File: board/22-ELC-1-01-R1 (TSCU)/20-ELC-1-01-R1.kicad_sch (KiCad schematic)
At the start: 10 parts, among them J1 Conn_01x116, J2 Conn_01x01, J3 Conn_01x06, J4 Conn_01x02, J5 Conn_01x02, J6 Conn_01x06, J7 Conn_01x01, U9 STM32F105RCTx

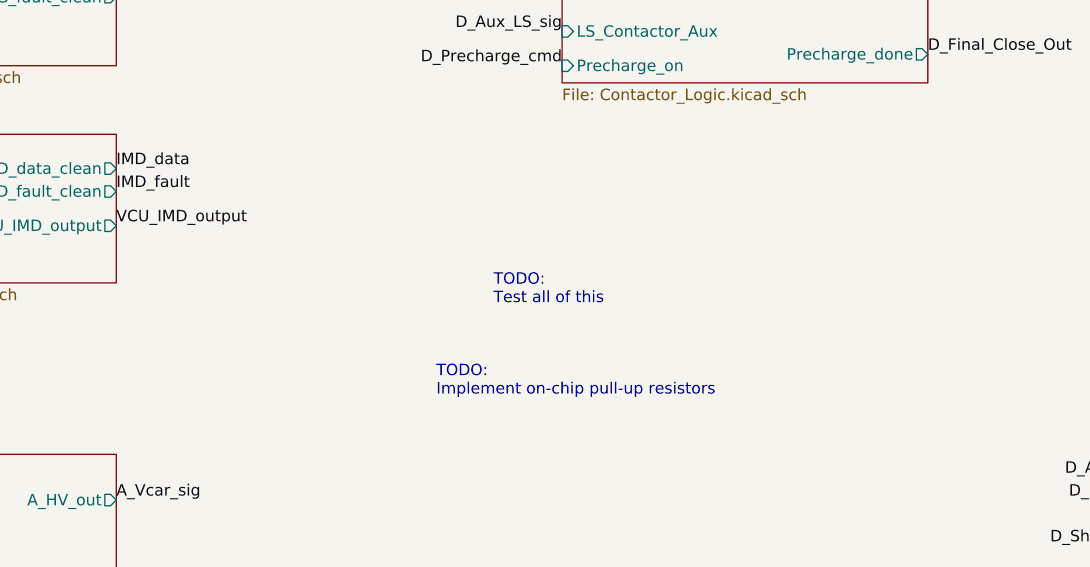
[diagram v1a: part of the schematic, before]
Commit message: Added few LEDs
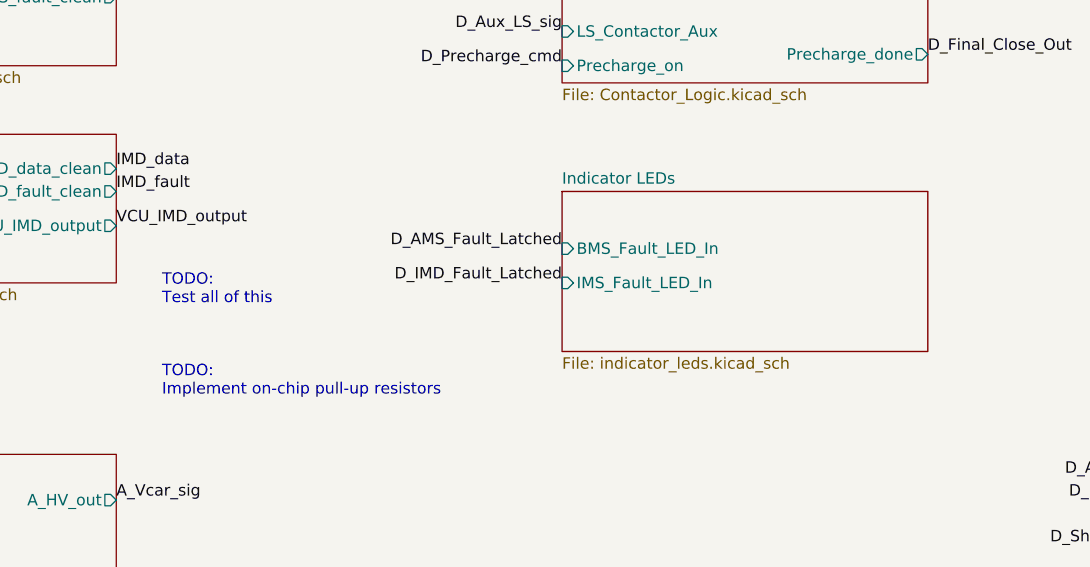
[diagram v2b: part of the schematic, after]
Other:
- added sheet Indicator LEDs (indicator_leds.kicad_sch)
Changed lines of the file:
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@@
     (stroke (width 0) (type default) (color 0 0 0 0))
   )
-  (text "TODO:\nTest all of this" (at 146.05 110.49 0)
+  (text "TODO:\nTest all of this" (at 109.22 110.49 0)
     (effects (font (size 1.27 1.27)) (justify left bottom))
   )
@@
     (effects (font (size 1.27 1.27)) (justify left bottom))
   )
-  (text "TODO:\nImplement on-chip pull-up resistors\n" (at 139.7 120.65 0)
+  (text "TODO:\nImplement on-chip pull-up resistors\n" (at 109.22 120.65 0)
     (effects (font (size 1.27 1.27)) (justify left bottom))
   )
@@
     (effects (font (size 1.27 1.27)) (justify right bottom))
   )
+  (label "D_AMS_Fault_Latched" (at 153.67 104.14 180)
+    (effects (font (size 1.27 1.27)) (justify right bottom))
+  )
   (label "dcdc_enable" (at 104.14 55.88 0)
     (effects (font (size 1.27 1.27)) (justify left bottom))
@@
   (label "IMD_KE" (at 29.21 116.84 0)
     (effects (font (size 1.27 1.27)) (justify left bottom))
+  )
+  (label "D_IMD_Fault_Latched" (at 153.67 107.95 180)
+    (effects (font (size 1.27 1.27)) (justify right bottom))
   )
   (label "D_Final_Close_Out" (at 194.31 82.55 0)
@@
     )
   )
+  (sheet (at 153.67 97.79) (size 40.64 17.78) (fields_autoplaced)
+    (stroke (width 0.1524) (type solid) (color 0 0 0 0))
+    (fill (color 0 0 0 0.0000))
+    (property "Sheet name" "Indicator LEDs" (id 0) (at 153.67 97.0784 0)
+      (effects (font (size 1.27 1.27)) (justify left bottom))
+    )
+    (property "Sheet file" "indicator_leds.kicad_sch" (id 1) (at 153.67 116.1546 0)
+      (effects (font (size 1.27 1.27)) (justify left top))
+    )
+    (pin "BMS_Fault_LED_In" input (at 153.67 104.14 180)
+      (effects (font (size 1.27 1.27)) (justify left))
+    )
+    (pin "IMS_Fault_LED_In" input (at 153.67 107.95 180)
+      (effects (font (size 1.27 1.27)) (justify left))
+    )
+  )
   (sheet_instances
     (path "/" (page "1"))
@@
     (path "/00000000-0000-0000-0000-00005d90d733" (page "11"))
     (path "/00000000-0000-0000-0000-000060f65a9c" (page "12"))
+    (path "/28d99f6e-a836-4db6-bc71-c35494bde910" (page "13"))
   )
   (symbol_instances
@@
       (reference "#PWR0106") (unit 1) (value "+5V") (footprint "")
     )
+    (path "/28d99f6e-a836-4db6-bc71-c35494bde910/24de73d2-9209-4edd-bd8a-39acaaf3a98b"
+      (reference "#PWR?") (unit 1) (value "GND") (footprint "")
+    )
+    (path "/28d99f6e-a836-4db6-bc71-c35494bde910/272d79de-c897-47ec-8cee-bdc709f98f7e"
+      (reference "#PWR?") (unit 1) (value "GND") (footprint "")
+    )
+    (path "/28d99f6e-a836-4db6-bc71-c35494bde910/90973fb4-d197-4463-9118-c7a94f62c78f"
+      (reference "#PWR?") (unit 1) (value "GND") (footprint "")
+    )
+    (path "/00000000-0000-0000-0000-0000617aed82/e9347cbc-281d-4d89-87e3-40eb1e5413f4"
+      (reference "#PWR?") (unit 1) (value "+5V") (footprint "")
+    )
+    (path "/28d99f6e-a836-4db6-bc71-c35494bde910/f395fc8e-933f-4544-83d1-7f8405023da7"
+      (reference "#PWR?") (unit 1) (value "+5V") (footprint "")
+    )
     (path "/00000000-0000-0000-0000-000060ed073e"
       (reference "A1") (unit 1) (value "Arduino_Nano_v3.x") (footprint "Module:Arduino_Nano")
@@
       (reference "D10") (unit 1) (value "B5819W") (footprint "Diode_SMD:D_SOD-123")
     )
+    (path "/00000000-0000-0000-0000-0000617aed82/3efac1eb-81f2-40fb-ac97-158176863b6e"
+      (reference "D?") (unit 1) (value "BMS_STATUS") (footprint "")
+    )
+    (path "/28d99f6e-a836-4db6-bc71-c35494bde910/5e5dc036-0bed-43f1-a5de-67433ad83c36"
+      (reference "D?") (unit 1) (value "BMS_FAULT_LED") (footprint "")
+    )
+    (path "/28d99f6e-a836-4db6-bc71-c35494bde910/dc6f94e1-4680-4b48-ace0-d6d0f492507b"
+      (reference "D?") (unit 1) (value "IMS_FAULT_LED") (footprint "")
+    )
     (path "/00000000-0000-0000-0000-00005d90d7d4/00000000-0000-0000-0000-00006038728c"
       (reference "F2") (unit 1) (value "2A") (footprint "Fuse:Fuse_1206_3216Metric_Pad1.42x1.75mm_HandSolder")
@@
       (reference "R51") (unit 1) (value "1k") (footprint "Resistor_SMD:R_0603_1608Metric_Pad0.98x0.95mm_HandSolder")
     )
+    (path "/28d99f6e-a836-4db6-bc71-c35494bde910/adac11e5-2860-40e4-bce4-e19a3e8a583d"
+      (reference "R?") (unit 1) (value "220") (footprint "")
+    )
+    (path "/00000000-0000-0000-0000-0000617aed82/b2b589bf-c37f-42c7-8186-328578765787"
+      (reference "R?") (unit 1) (value "220") (footprint "")
+    )
+    (path "/28d99f6e-a836-4db6-bc71-c35494bde910/eedced55-176a-45b3-a3da-bff1a25d967f"
+      (reference "R?") (unit 1) (value "220") (footprint "")
+    )
     (path "/00000000-0000-0000-0000-000060f320ba/00000000-0000-0000-0000-0000600d193f"
       (reference "RV1") (unit 1) (value "R_POT_TRIM") (footprint "Potentiometer_THT:Potentiometer_Bourns_3296W_Vertical")
@@
       (reference "TP18") (unit 1) (value "TestPoint") (footprint "TestPoint:TestPoint_THTPad_D1.0mm_Drill0.5mm")
     )
+    (path "/00000000-0000-0000-0000-00005d90d733/ebf6a852-e42b-44f6-a1de-740340178ead"
+      (reference "TP?") (unit 1) (value "TestPoint") (footprint "")
+    )
     (path "/00000000-0000-0000-0000-00005d9ae4f9/00000000-0000-0000-0000-000060f3ae0d"
       (reference "U1") (unit 1) (value "TPS5430DDA") (footprint "Package_SO:TI_SO-PowerPAD-8_ThermalVias")
@@
       (reference "U14") (unit 3) (value "LM358") (footprint "Package_SO:SOIC-8_3.9x4.9mm_P1.27mm")
     )
+    (path "/28d99f6e-a836-4db6-bc71-c35494bde910/99db8223-dc3d-4d3f-8640-b6a4b37188a4"
+      (reference "U?") (unit 1) (value "LM358") (footprint "")
+    )
+    (path "/28d99f6e-a836-4db6-bc71-c35494bde910/e0bcac9d-dab7-4abe-89f1-620c9ec5fd7a"
+      (reference "U?") (unit 1) (value "LM358") (footprint "")
+    )
+    (path "/28d99f6e-a836-4db6-bc71-c35494bde910/13ca8184-2714-4986-b99a-1f20e984bbea"
+      (reference "U?") (unit 2) (value "LM358") (footprint "")
+    )
+    (path "/28d99f6e-a836-4db6-bc71-c35494bde910/6a060a57-d1e4-464a-b390-6294ef420732"
+      (reference "U?") (unit 3) (value "LM358") (footprint "")
+    )
     (path "/00000000-0000-0000-0000-000060f545d6/00000000-0000-0000-0000-000060f58487"

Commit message: More work
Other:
- added sheet Untitled Sheet (../../2023KicadLibrary/Standardized Subsheets/microcontroller.kicad_sch)

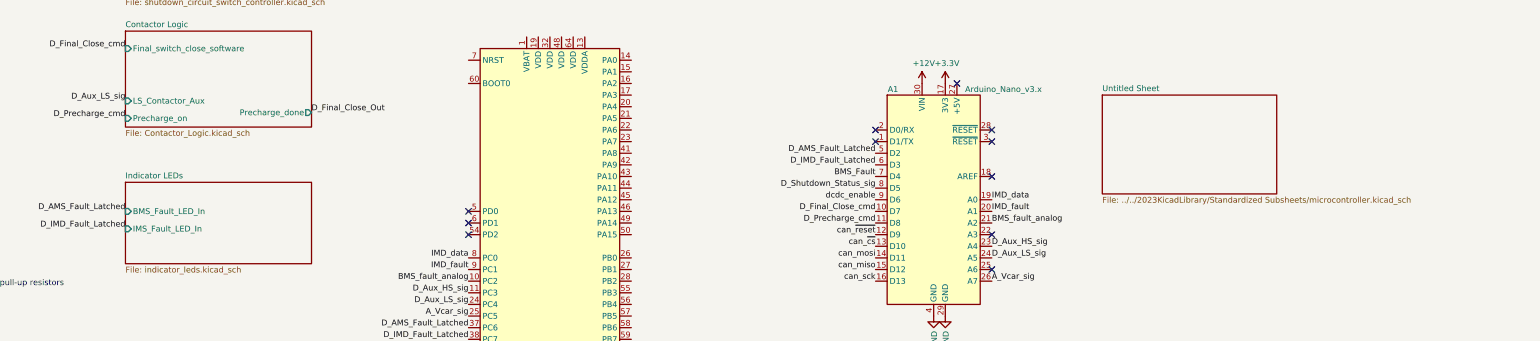
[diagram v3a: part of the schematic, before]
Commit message: More LEDs and test points
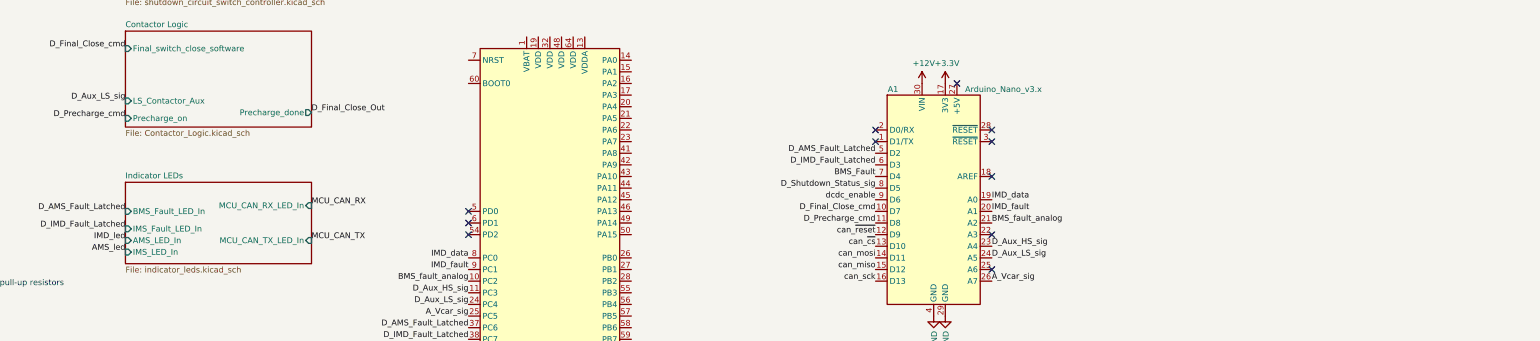
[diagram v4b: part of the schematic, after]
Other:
- removed sheet Untitled Sheet
- sheet Indicator LEDs ports: added AMS_LED_In, IMS_LED_In, MCU_CAN_RX_LED_In, MCU_CAN_TX_LED_In; removed none

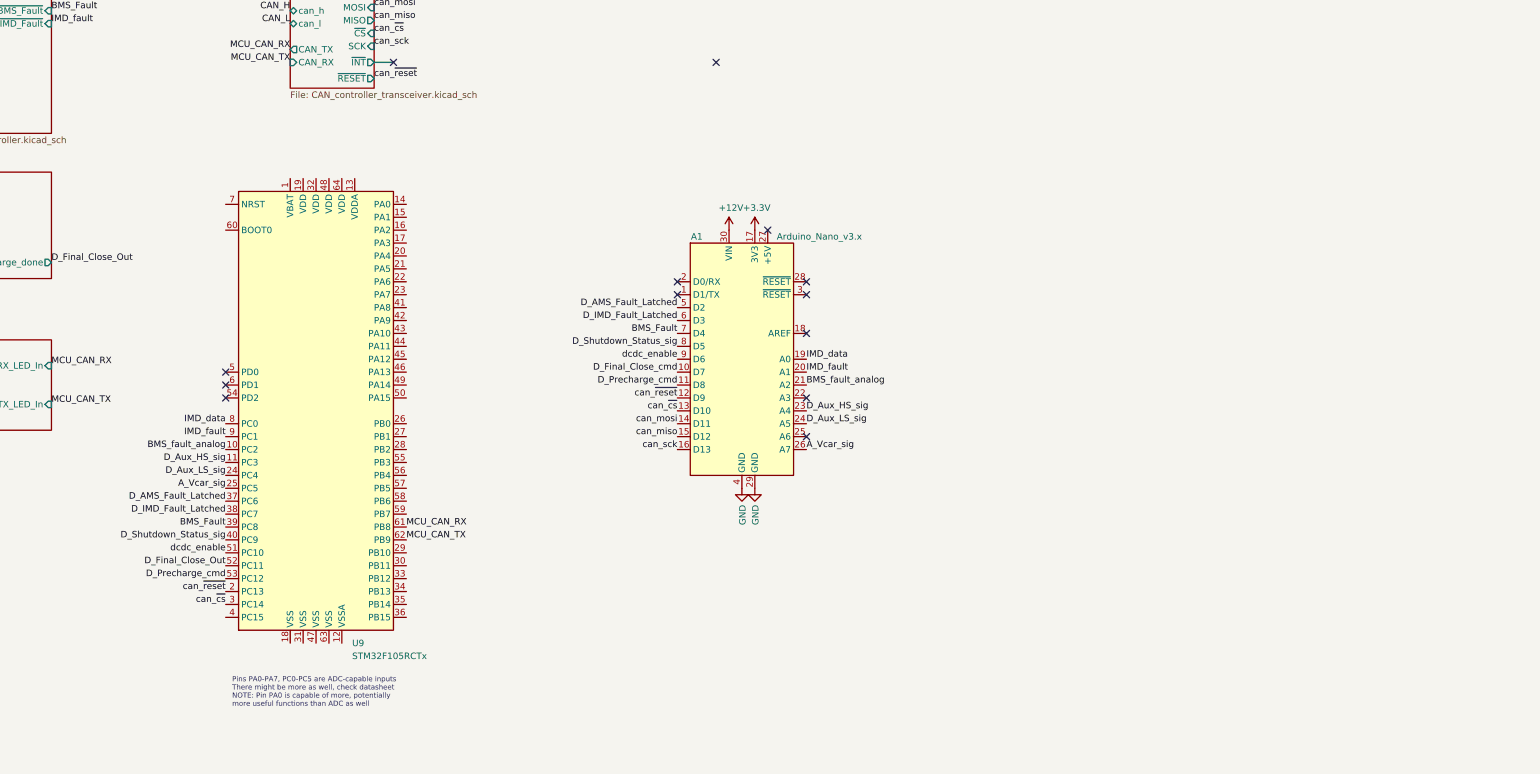
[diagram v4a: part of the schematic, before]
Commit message: More LEDs and TPs
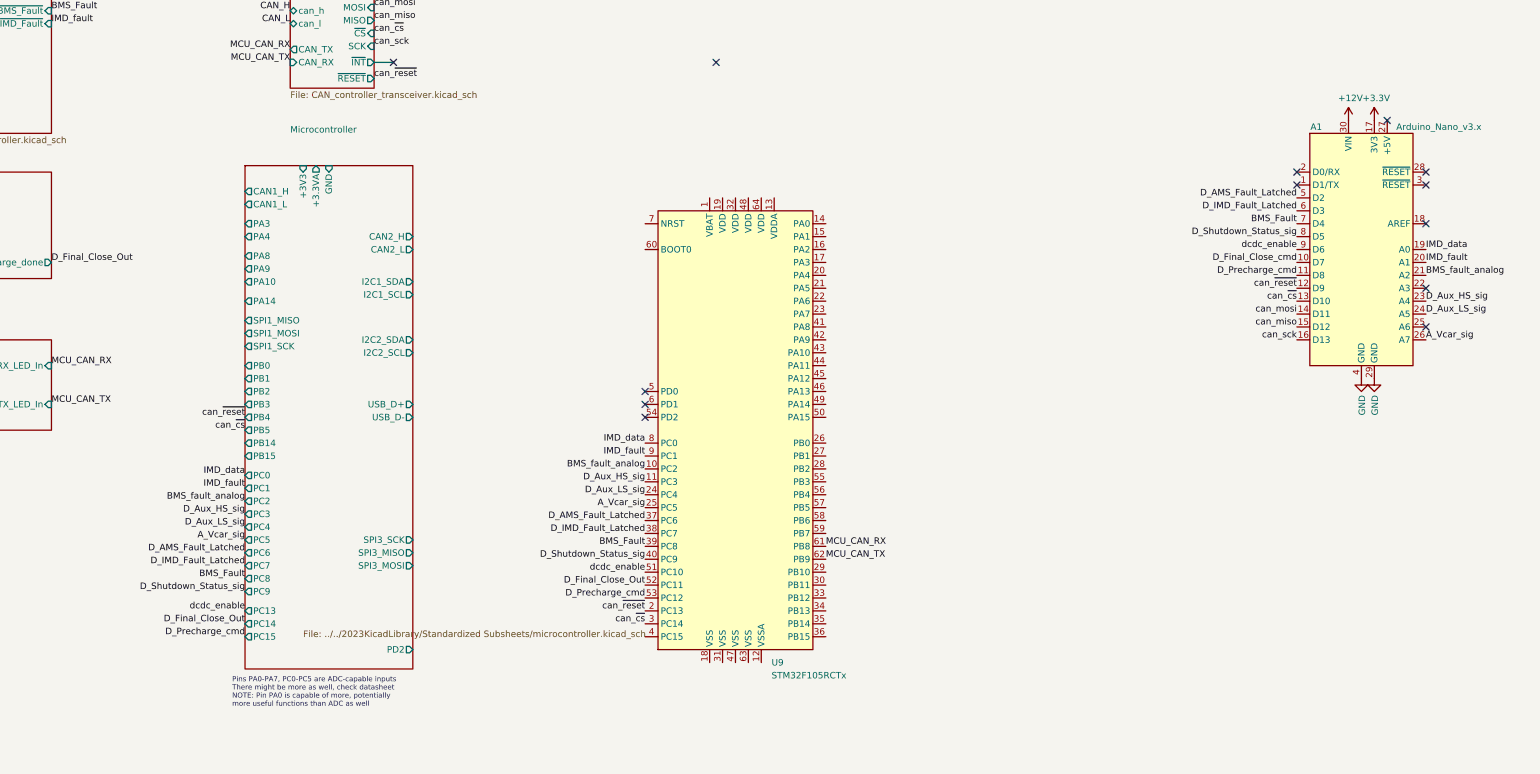
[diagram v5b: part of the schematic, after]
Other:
- added sheet Microcontroller (../../2023KicadLibrary/Standardized Subsheets/microcontroller.kicad_sch)
- moved on the sheet: A1, U9

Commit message: Ready for review
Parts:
- removed A1: Arduino_Nano_v3.x, Module:Arduino_Nano, symbol MCU_Module:Arduino_Nano_v2.x
- removed U9: STM32F105RCTx, Package_QFP:LQFP-64_10x10mm_P0.5mm, symbol MCU_ST_STM32F1:STM32F105RCTx
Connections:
- no-connect marks 15 -> 33
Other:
- added sheet 3V3Supply (../../2023KicadLibrary/Standardized Subsheets/LDO.kicad_sch)
- sheet Indicator LEDs ports: added Final_Precharge_Close_Out_LED_In, Precharge_CMD_LED_In; removed MCU_CAN_RX_LED_In, MCU_CAN_TX_LED_In
- sheet Microcontroller ports: added +5V; removed none

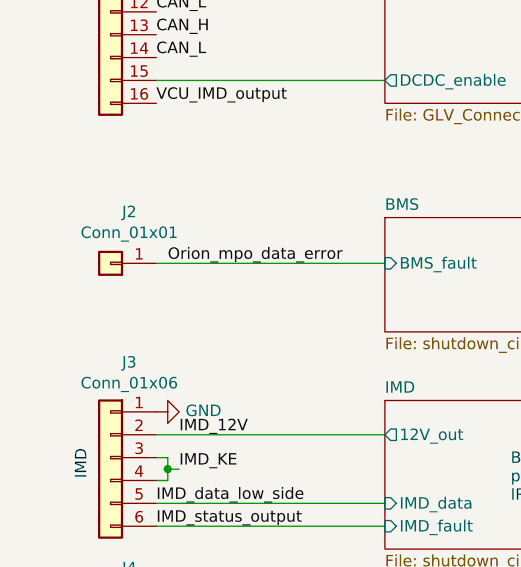
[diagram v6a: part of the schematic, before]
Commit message: All good except need to switch everything to accepting 24v power
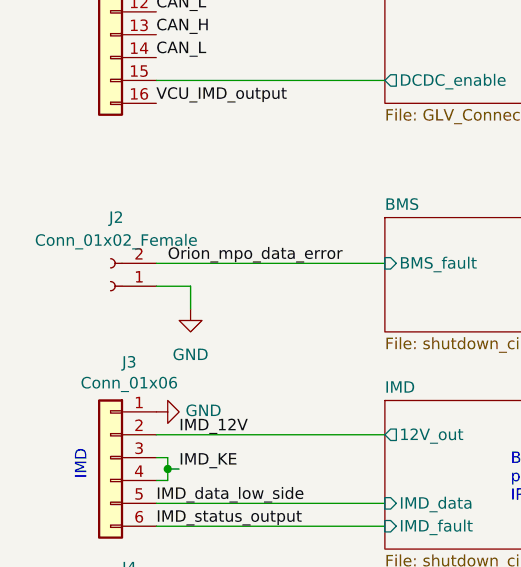
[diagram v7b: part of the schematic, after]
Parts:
- removed J2: Conn_01x01, symbol Connector_Generic:Conn_01x01
- added J2: Conn_01x02_Female, Connector_Molex:Molex_Micro-Fit_3.0_43650-0200_1x02_P3.00mm_Horizontal, symbol Connector:Conn_01x02_Female
- J1: footprint Connector_Molex:Molex_Micro-Fit_3.0_43045-1612_2x08_P3.00mm_Vertical -> Connector_Molex:Molex_Micro-Fit_3.0_43045-1600_2x08_P3.00mm_Horizontal
- J5: footprint (none) -> Connector_Molex:Molex_Micro-Fit_3.0_43045-0200_2x01_P3.00mm_Horizontal
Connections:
- net GND: now also J2.1 (Pin_1)
- net Orion_mpo_data_error: now also J2.2 (Pin_2)
